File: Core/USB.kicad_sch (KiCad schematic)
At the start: 16 parts, among them J5 USB_C_Receptacle_USB2.0

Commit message: Update metadata
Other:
- company: (none) -> GuavTek
- title: (none) -> M2IDI - USB CORE
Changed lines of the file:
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@@
 (kicad_sch (version 20230121) (generator eeschema)
   (paper "A4")
+  (title_block
+    (title "M2IDI - USB CORE")
+    (date "2023-06-18")
+    (rev "2.0")
+    (company "GuavTek")
+  )
   (junction (at 86.995 57.785) (diameter 0) (color 0 0 0 0)
   )

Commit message: Add optional solder bridge++
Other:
- note added: "This resistor should be 0,5% tolerance, but 1% is fine"
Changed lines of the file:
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@@
     (stroke (width 0) (type default))
+  )
+  (text "This resistor should \nbe 0,5% tolerance,\nbut 1% is fine"
+    (at 104.14 118.11 0)
+    (effects (font (size 1.27 1.27)) (justify left bottom))
   )
   (global_label "USB_ID" (shape output) (at 73.025 91.44 180)

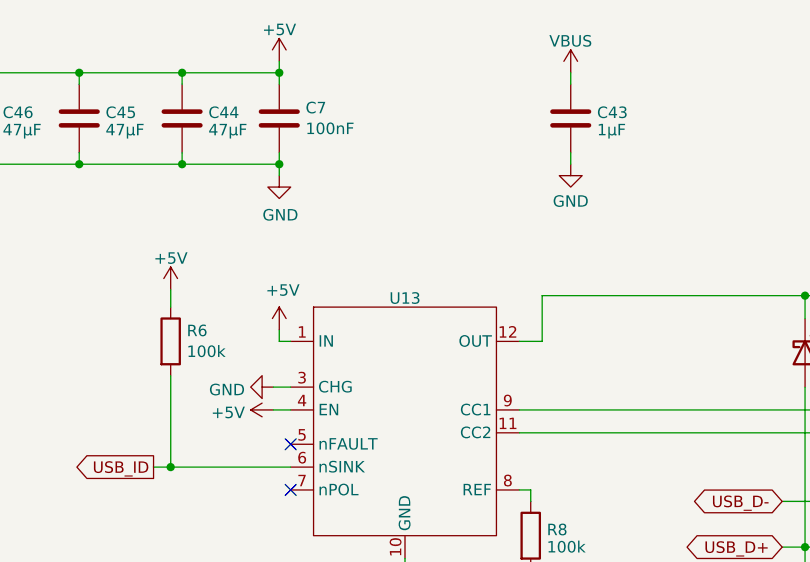
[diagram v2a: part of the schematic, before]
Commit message: Change CAN tranceiver to MCP2562
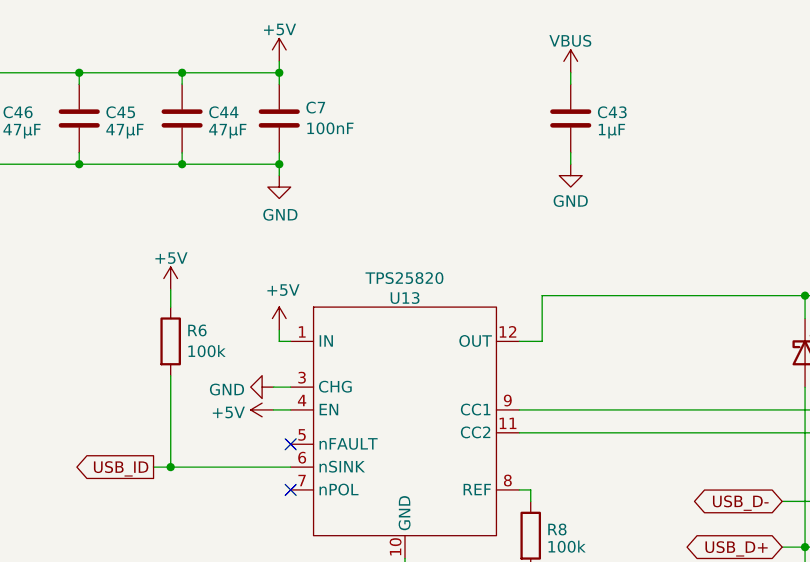
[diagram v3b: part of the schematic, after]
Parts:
- U13: value ~ -> TPS25820
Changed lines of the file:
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@@
   )
   (symbol (lib_id "Custom_Sym:TPS25820") (at 100.965 86.36 0) (unit 1)
-    (in_bom yes) (on_board yes) (dnp no) (fields_autoplaced)
+    (in_bom yes) (on_board yes) (dnp no)
     (property "Reference" "U13" (at 100.965 72.6981 0)
       (effects (font (size 1.27 1.27)))
     )
-    (property "Value" "~" (at 100.965 86.36 0)
+    (property "Value" "TPS25820" (at 100.965 70.485 0)
       (effects (font (size 1.27 1.27)))
     )

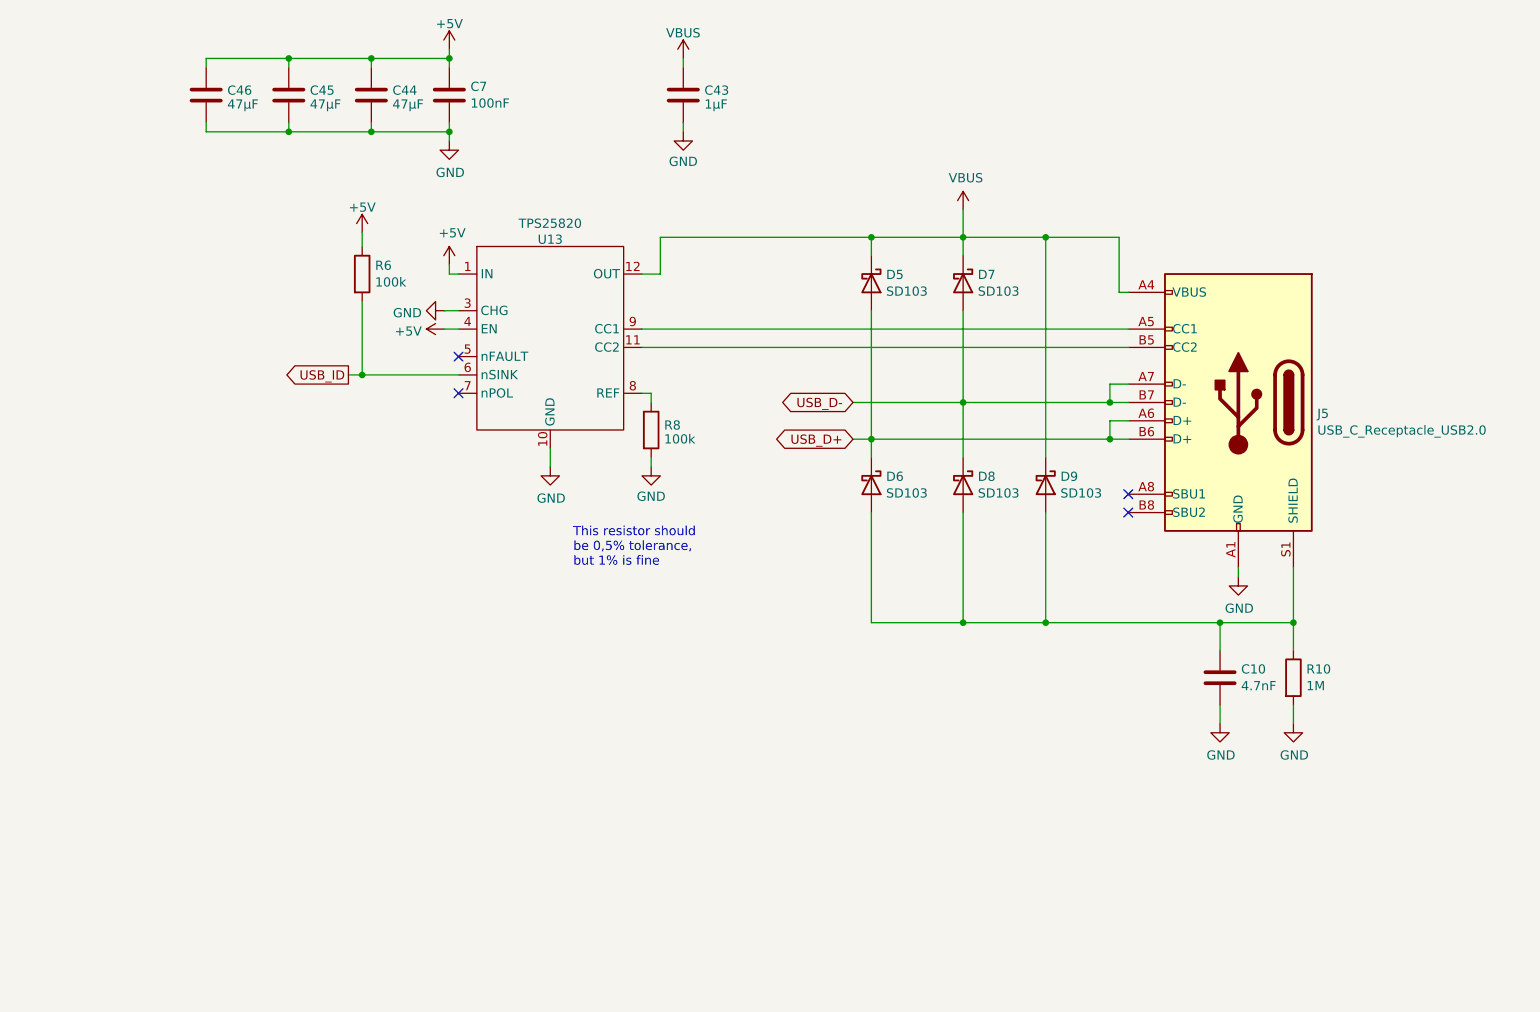
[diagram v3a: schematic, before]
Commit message: Change USB id chips to TUSB321 and MID2005
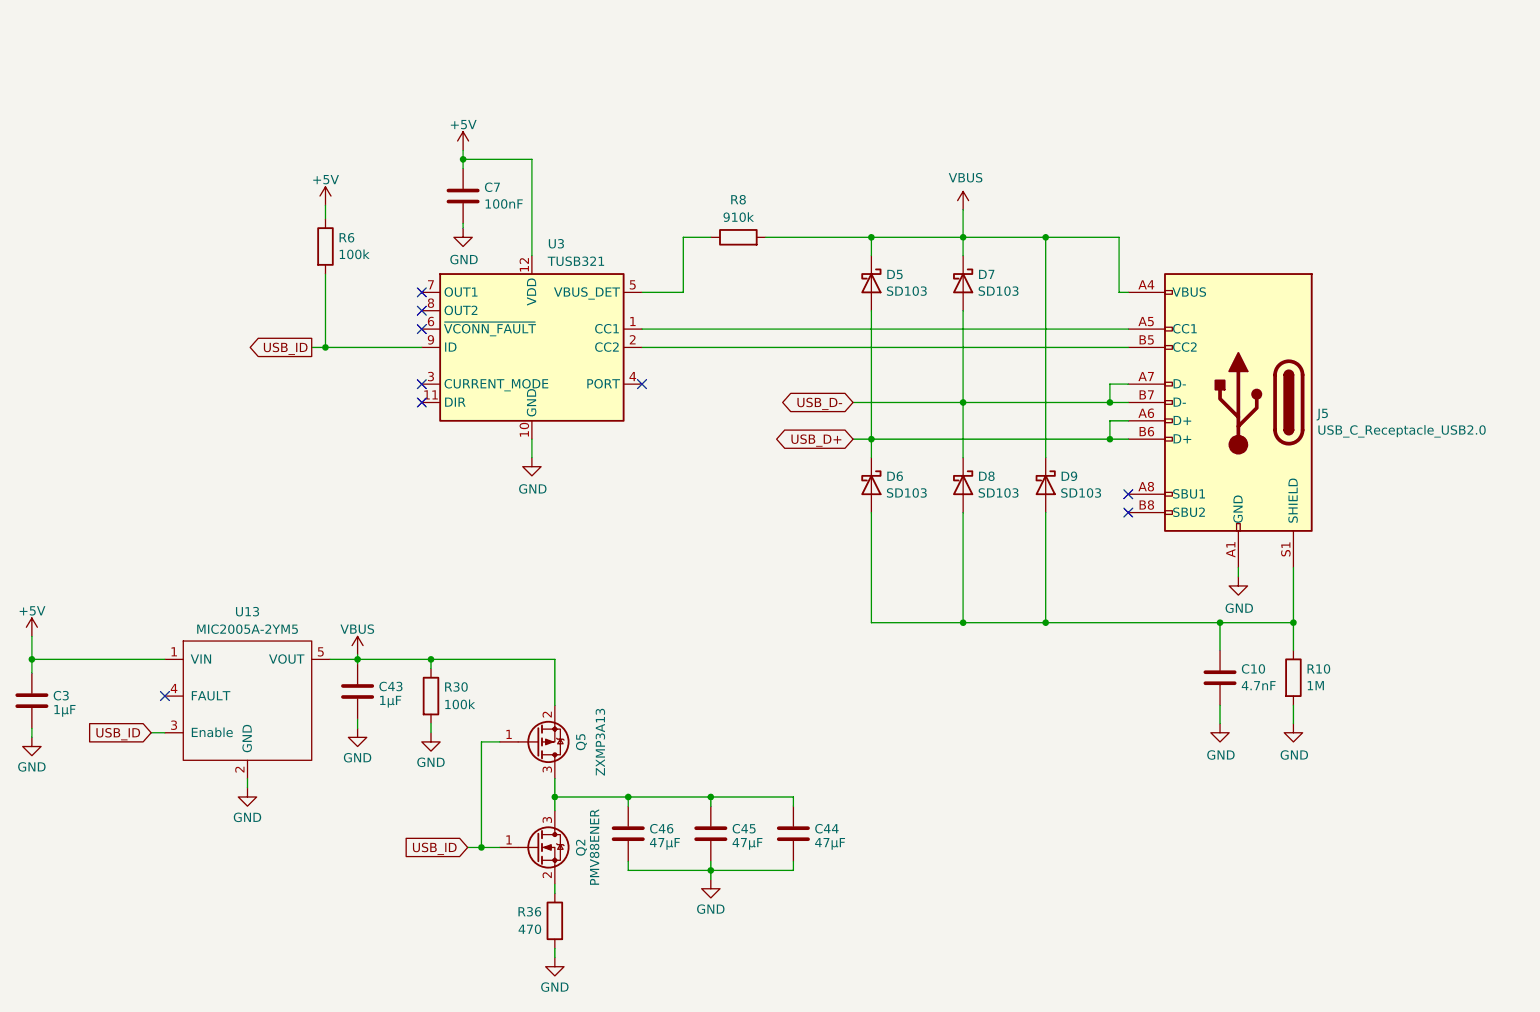
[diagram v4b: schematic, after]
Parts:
- removed U13: TPS25820, Package_SON:WSON-12-1EP_3x2mm_P0.5mm_EP1x2.65, symbol Custom_Sym:TPS25820
- added C3: 1µF, Capacitor_SMD:C_0603_1608Metric, symbol Device:C
- added Q2: PMV88ENER, Package_TO_SOT_SMD:SOT-23, symbol Device:Q_NMOS_GSD
- added Q5: ZXMP3A13, Package_TO_SOT_SMD:SOT-23, symbol Device:Q_PMOS_GSD
- added R30: 100k, Resistor_SMD:R_0603_1608Metric, symbol Device:R
- added R36: 470, Resistor_SMD:R_0603_1608Metric, symbol Device:R
- added U13: MIC2005A-2YM5, Package_TO_SOT_SMD:SOT-23-5, symbol Custom_Sym:MIC2005
- added U3: TUSB321, Package_DFN_QFN:Texas_X2QFN-12_1.6x1.6mm_P0.4mm, symbol Interface_USB:TUSB321
- R8: value 100k -> 910k
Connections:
- net +5V: now also C3.1, U13.1 (VIN), U3.12 (VDD); no longer C44.1, C45.1, C46.1
- net GND: now also C3.2, R30.2, R36.2, U13.2 (GND), U3.10 (GND); no longer R8.2
- net USB_ID: now also Q2.1 (G), Q5.1 (G), U13.3 (Enable), U3.9 (ID)
- net VBUS: now also R8.2, Q5.2 (S), R30.1, U13.5 (VOUT)
- net at J5.A5 (CC1): now also U3.1 (CC1)
- net at J5.B5 (CC2): now also U3.2 (CC2)
- net at R8.1: now also U3.5 (VBUS_DET)
- new net: Q2.2 (S), R36.1
- new net: C44.1, C45.1, C46.1, Q2.3 (D), Q5.3 (D)
- no-connect marks 4 -> 9
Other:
- note removed: "This resistor should be 0,5% tolerance, but 1% is fine"
- moved on the sheet: C43, C44, C45, C46, C7, R6, R8
